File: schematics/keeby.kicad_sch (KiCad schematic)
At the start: 58 parts, among them SW1 SW_Push, SW10 SW_Push, SW11 SW_Push, SW12 SW_Push, SW13 SW_Push, SW14 SW_Push, SW15 SW_Push, SW16 SW_Push, SW17 SW_Push, SW18 SW_Push, SW19 SW_Push, SW2 SW_Push, SW20 SW_Push, SW21 SW_Push, SW22 SW_Push, SW23 SW_Push, SW24 SW_Push, SW25 SW_Push, SW26 SW_Push, SW27 SW_Push, SW28 SW_Push, SW3 SW_Push, SW4 SW_Push, SW5 SW_Push, SW6 SW_Push, SW7 SW_Push, SW8 SW_Push, SW9 SW_Push

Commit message: journaling + more schematic
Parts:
- added D29, D30, D31, D32, D33, D34, D35, D36, D37, D38, D39, D40, D41, D42, D43, D44, D45, D46, D47, D48, D49, D50, D51, D52, D53, D54, D55, D56, D57, D58, D59, D61, D63, D65, D67, D68, D69, D70, D71: 1N4148, Diode_THT:D_DO-35_SOD27_P7.62mm_Horizontal, symbol Diode:1N4148
- added H1, H2, H3, H4: MountingHole, symbol Mechanical:MountingHole
- added S2, S3, S4: MX_stab, PCM_marbastlib-mx:STAB_MX_P_6.25u, symbol PCM_marbastlib-mx:MX_stab
- added SW29, SW30, SW31, SW32, SW33, SW34, SW35, SW36, SW37, SW38, SW39, SW40, SW41, SW42, SW43, SW44, SW45, SW46, SW47, SW48, SW49, SW50, SW51, SW52, SW53, SW54, SW55, SW56, SW57, SW58, SW59, SW61, SW63, SW65, SW67, SW68, SW69, SW70, SW71: SW_Push, symbol Switch:SW_Push
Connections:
- net COL0: now reaches SW1.1
- net COL0: now also A1.7 (GPIO5), SW15.1, SW29.1, SW43.1, SW57.1
- net ROW0: now reaches A1.1 (GPIO0)
- net ROW1: now reaches A1.2 (GPIO1)
- net ROW3: now reaches A1.4 (GPIO2)
- net ROW4: now reaches A1.5 (GPIO3)
- net ROW5: now reaches A1.6 (GPIO4)
- new net: D30.2 (A), SW30.2
- new net: D43.2 (A), SW43.2
- new net: D52.2 (A), SW52.2
- new net: D35.2 (A), SW35.2
- new net: D51.2 (A), SW51.2
- new net: D36.2 (A), SW36.2
- new net: D71.2 (A), SW71.2
- new net: D48.2 (A), SW48.2
- new net: D46.2 (A), SW46.2
- new net: D67.2 (A), SW67.2
- new net: D47.2 (A), SW47.2
- new net: D34.2 (A), SW34.2
- new net: D57.2 (A), SW57.2
- new net: D45.2 (A), SW45.2
- new net: D38.2 (A), SW38.2
- new net: D44.2 (A), SW44.2
- new net: D55.2 (A), SW55.2
- new net: D49.2 (A), SW49.2
- new net: D42.2 (A), SW42.2
- new net: D32.2 (A), SW32.2
- new net: D40.2 (A), SW40.2
- new net: D61.2 (A), SW61.2
- new net: D56.2 (A), SW56.2
- new net: D65.2 (A), SW65.2
- new net: D37.2 (A), SW37.2
- new net: D68.2 (A), SW68.2
- new net: D63.2 (A), SW63.2
- new net: D39.2 (A), SW39.2
- new net: D41.2 (A), SW41.2
- new net: D53.2 (A), SW53.2
- new net: D54.2 (A), SW54.2
- new net: D50.2 (A), SW50.2
- new net: D70.2 (A), SW70.2
- new net: D31.2 (A), SW31.2
- new net: D33.2 (A), SW33.2
- new net: D59.2 (A), SW59.2
- new net: D29.2 (A), SW29.2
- new net: D69.2 (A), SW69.2
- new net: D58.2 (A), SW58.2
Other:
- moved on the sheet: A1, D1, D10, D11, D12, D13, D14, D15, D16, D17, D18, D19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

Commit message: hjalp vro
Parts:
- A1: footprint Module:RaspberryPi_Pico_Common_Unspecified -> Module:RaspberryPi_Pico_Common_THT
- S1, S2, S3, S4: footprint PCM_marbastlib-mx:STAB_MX_P_6.25u -> PCM_marbastlib-mx:STAB_MX_2.25u
- SW1, SW10, SW11, SW12, SW13, SW14, SW15, SW16, SW17, SW18, SW19, SW2, SW20, SW21, SW22, SW23, SW24, SW25, SW26, SW27, SW28, SW29, SW3, SW30, SW31, SW32, SW33, SW34, SW35, SW36, SW37, SW38, SW39, SW4, SW40, SW41, SW42, SW43, SW44, SW45, SW46, SW47, SW48, SW49, SW5, SW50, SW51, SW52, SW53, SW54, SW55, SW56, SW57, SW58, SW59, SW6, SW61, SW63, SW65, SW67, SW68, SW69, SW7, SW70, SW71, SW8, SW9: footprint (none) -> PCM_marbastlib-mx:SW_MX_1u
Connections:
- net ROW0: now also D1.1 (K), D10.1 (K), D11.1 (K), D12.1 (K), D13.1 (K), D14.1 (K), D2.1 (K), D3.1 (K), D4.1 (K), D5.1 (K), D6.1 (K), D7.1 (K), D8.1 (K), D9.1 (K)
- net ROW1: now also D15.1 (K), D16.1 (K), D17.1 (K), D18.1 (K), D19.1 (K), D20.1 (K), D21.1 (K), D22.1 (K), D23.1 (K), D24.1 (K), D25.1 (K), D26.1 (K), D27.1 (K), D28.1 (K)
- net ROW3: now also D29.1 (K), D30.1 (K), D31.1 (K), D32.1 (K), D33.1 (K), D34.1 (K), D35.1 (K), D36.1 (K), D37.1 (K), D38.1 (K), D39.1 (K), D40.1 (K), D41.1 (K), D42.1 (K)
- net ROW4: now also D43.1 (K), D44.1 (K), D45.1 (K), D46.1 (K), D47.1 (K), D48.1 (K), D49.1 (K), D50.1 (K), D51.1 (K), D52.1 (K), D53.1 (K), D54.1 (K), D55.1 (K), D56.1 (K)
- net ROW5: now also D57.1 (K), D58.1 (K), D59.1 (K), D61.1 (K), D63.1 (K), D65.1 (K), D67.1 (K), D68.1 (K), D69.1 (K), D70.1 (K), D71.1 (K)
- net COL1: now reaches SW30.1
- net COL1: now also A1.9 (GPIO6), SW16.1, SW2.1, SW44.1, SW58.1
- net COL2: now reaches SW45.1
- net COL2: now also A1.10 (GPIO7), SW17.1, SW3.1, SW31.1, SW59.1
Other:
- moved on the sheet: A1

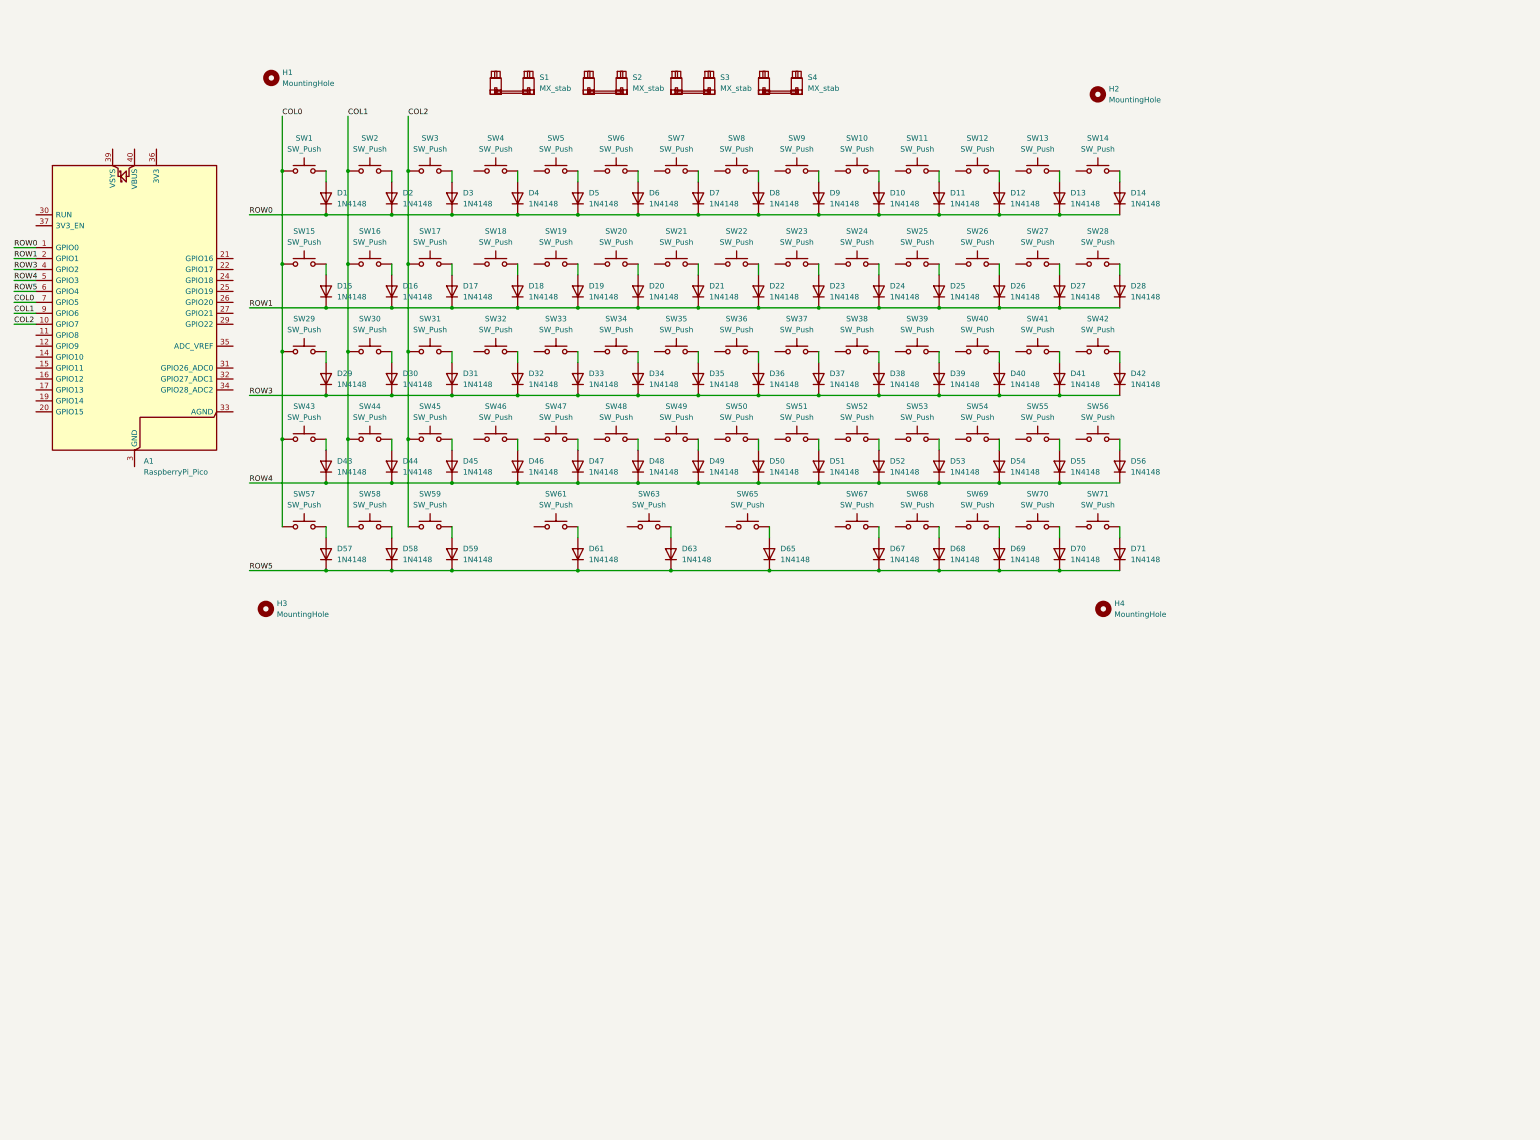
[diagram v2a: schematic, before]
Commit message: 15 columns and 5 rows
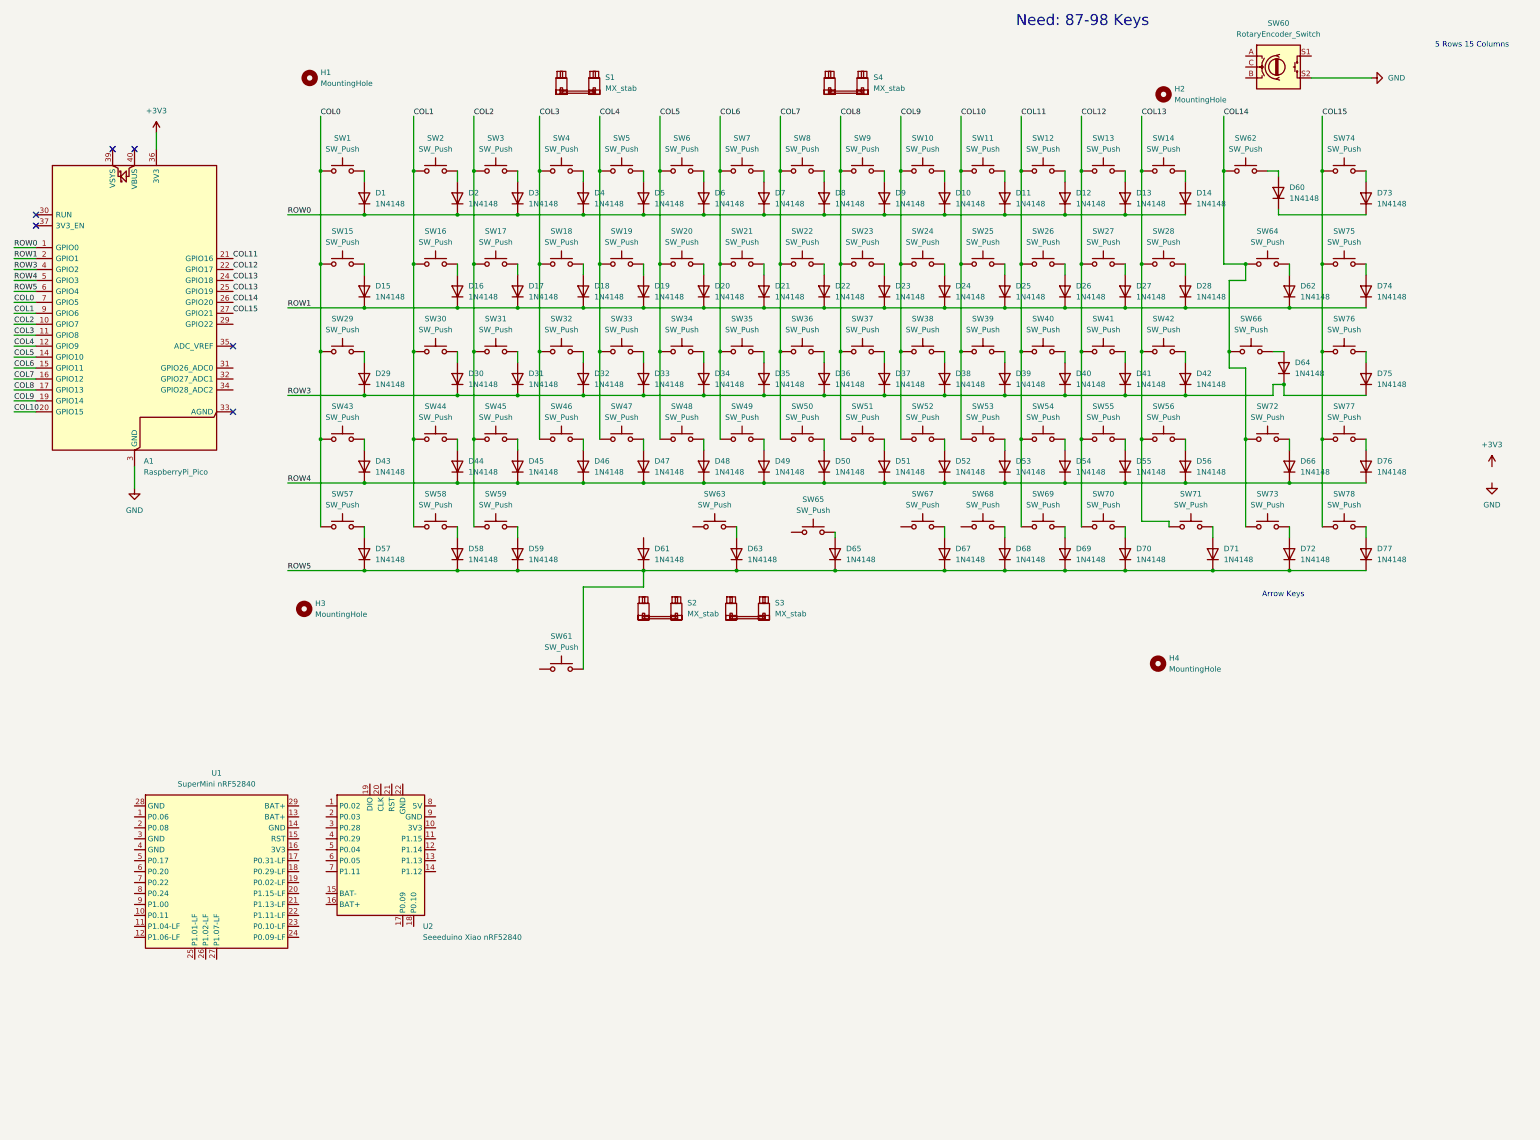
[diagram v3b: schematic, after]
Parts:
- added D60, D62, D64, D66, D72, D73, D74, D75, D76, D77: 1N4148, Diode_THT:D_DO-35_SOD27_P7.62mm_Horizontal, symbol Diode:1N4148
- added SW60: RotaryEncoder_Switch, symbol Device:RotaryEncoder_Switch
- added SW62, SW64, SW66, SW72, SW73, SW74, SW75, SW76, SW77, SW78: SW_Push, PCM_marbastlib-mx:SW_MX_1u, symbol Switch:SW_Push
- added U1: SuperMini nRF52840, PCM_marbastlib-xp-promicroish:SuperMini_nRF52840_AH_USBup, symbol PCM_marbastlib-promicroish:SuperMini_nRF52840
- added U2: Seeeduino Xiao nRF52840, PCM_marbastlib-xp-promicroish:Xiao_nRF52840_ACH, symbol PCM_marbastlib-promicroish:Seeeduino_Xiao_nRF52840
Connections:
- net ROW1: now also D62.1 (K), D74.1 (K)
- net ROW3: now also D64.1 (K), D75.1 (K)
- net ROW4: now also D66.1 (K), D76.1 (K)
- net ROW5: now also SW61.2, D72.1 (K), D77.1 (K)
- net COL9: now reaches SW52.1
- net COL9: now also A1.19 (GPIO14), SW10.1, SW24.1, SW38.1
- net COL3: now reaches SW18.1
- net COL3: now also A1.11 (GPIO8), SW32.1, SW4.1, SW46.1
- net COL8: now reaches SW51.1
- net COL8: now also A1.17 (GPIO13), SW23.1, SW37.1, SW9.1
- net COL7: now reaches SW36.1
- net COL7: now also A1.16 (GPIO12), SW22.1, SW50.1, SW8.1
- net COL4: now reaches SW47.1
- net COL4: now also A1.12 (GPIO9), SW19.1, SW33.1, SW5.1
- net COL6: now reaches SW7.1
- net COL6: now also A1.15 (GPIO11), SW21.1, SW35.1, SW49.1
- net COL12: now reaches SW13.1
- net COL12: now also A1.22 (GPIO17), SW27.1, SW41.1, SW55.1, SW70.1
- net COL11: now reaches SW12.1
- net COL11: now also A1.21 (GPIO16), SW26.1, SW40.1, SW54.1, SW69.1
- net COL13: now reaches SW42.1
- net COL13: now also A1.24 (GPIO18), A1.25 (GPIO19), SW14.1, SW28.1, SW56.1, SW71.1
- net at D61.2 (A): no longer SW61.2
- net COL10: now reaches SW39.1
- net COL10: now also A1.20 (GPIO15), SW11.1, SW25.1, SW53.1
- net COL5: now reaches SW48.1
- net COL5: now also A1.14 (GPIO10), SW20.1, SW34.1, SW6.1
- net GND: now reaches A1.13 (GND), A1.18 (GND), A1.23 (GND), A1.28 (GND), A1.3 (GND), A1.38 (GND), A1.8 (GND)
- net GND: now also SW60.S2
- net COL14: now reaches A1.26 (GPIO20)
- net COL14: now also SW62.1, SW64.1, SW66.1, SW72.1, SW73.1
- net COL15: now reaches A1.27 (GPIO21)
- net COL15: now also SW74.1, SW75.1, SW76.1, SW77.1, SW78.1
- net +3V3: now reaches A1.36 (3V3)
- new net: D62.2 (A), SW64.2
- new net: D72.2 (A), SW73.2
- new net: D64.2 (A), SW66.2
- new net: D66.2 (A), SW72.2
- new net: D60.2 (A), SW62.2
- new net: D75.2 (A), SW76.2
- new net: D74.2 (A), SW75.2
- new net: D60.1 (K), D73.1 (K)
- new net: D73.2 (A), SW74.2
- new net: D77.2 (A), SW78.2
- new net: D76.2 (A), SW77.2
- no-connect marks 0 -> 6
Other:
- note added: "5 Rows 15 Columns"
- note added: "Arrow Keys"
- note added: "Need: 87-98 Keys"
- moved on the sheet: D1, D10, D11, D12, D13, D14, D15, D16, D17, D18, D19, D2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

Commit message: laid out this ratnest is hurting my brain
installed kbplacer to do ts
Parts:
- removed D61, D65: 1N4148, Diode_THT:D_DO-35_SOD27_P7.62mm_Horizontal, symbol Diode:1N4148
- removed SW61, SW65: SW_Push, PCM_marbastlib-mx:SW_MX_1u, symbol Switch:SW_Push
- removed U2: Seeeduino Xiao nRF52840, PCM_marbastlib-xp-promicroish:Xiao_nRF52840_ACH, symbol PCM_marbastlib-promicroish:Seeeduino_Xiao_nRF52840
- added D76, D77: SK6812MINI-E, LED_SMD:LED_SK6812MINI-E_3.2x2.8mm_P1.5mm_ReverseMount, symbol LED:SK6812MINI-E
- added D78: SK6812MINI-E, SK6812MINI-E - 3.2x2.8x1.78mm, symbol SK6812MINI-E:SK6812MINI-E
- added LED1: SK6812MINI-E, PCM_marbastlib-various:LED_6028R, symbol PCM_marbastlib-various:SK6812MINI-E
- S3: footprint PCM_marbastlib-mx:STAB_MX_2.25u -> PCM_marbastlib-mx:STAB_MX_6.25u
- SW76: renamed from SW60; footprint (none) -> PCM_marbastlib-various:ROT_Alps_EC11E-Switch
- renumbered D60 to D1, D9 to D10, D10 to D11, D11 to D12, D12 to D13, D13 to D14, D14 to D15, D73 to D16, D15 to D17, D16 to D18, D17 to D19, D1 to D2, D18 to D20, D19 to D21, D20 to D22, D21 to D23, D22 to D24, D23 to D25, D24 to D26, D25 to D27, D26 to D28, D27 to D29, D2 to D3, D28 to D30, D62 to D31, D74 to D32, D64 to D33, D29 to D34, D30 to D35, D31 to D36, D32 to D37, D33 to D38, D34 to D39, D3 to D4, D35 to D40, D36 to D41, D37 to D42, D38 to D43, D39 to D44, D40 to D45, D41 to D46, D42 to D47, D75 to D48, D43 to D49, D4 to D5, D44 to D50, D45 to D51, D46 to D52, D47 to D53, D48 to D54, D49 to D55, D50 to D56, D51 to D57, D52 to D58, D53 to D59, D5 to D6, D54 to D60, D55 to D61, D56 to D62, D66 to D63, D76 to D64, D57 to D65, D58 to D66, D59 to D67, D63 to D68, D67 to D69, D6 to D7, D68 to D70, D69 to D71, D70 to D72, D71 to D73, D72 to D74, D77 to D75, D7 to D8, D8 to D9, S4 to S2, S2 to S4, SW62 to SW15, SW74 to SW16, SW15 to SW17, SW16 to SW18, SW17 to SW19, SW18 to SW20, SW19 to SW21, SW20 to SW22, SW21 to SW23, SW22 to SW24, SW23 to SW25, SW24 to SW26, SW25 to SW27, SW26 to SW28, SW27 to SW29, SW28 to SW30, SW64 to SW31, SW75 to SW32, SW29 to SW33, SW30 to SW34, SW31 to SW35, SW32 to SW36, SW33 to SW37, SW34 to SW38, SW35 to SW39, SW36 to SW40, SW37 to SW41, SW38 to SW42, SW39 to SW43, SW40 to SW44, SW41 to SW45, SW42 to SW46, SW66 to SW47, SW76 to SW48, SW43 to SW49, SW44 to SW50, SW45 to SW51, SW46 to SW52, SW47 to SW53, SW48 to SW54, SW49 to SW55, SW50 to SW56, SW51 to SW57, SW52 to SW58, SW53 to SW59, SW54 to SW60, SW55 to SW61, SW56 to SW62, SW72 to SW63, SW77 to SW64, SW57 to SW65, SW58 to SW66, SW59 to SW67, SW63 to SW68, SW67 to SW69, SW68 to SW70, SW69 to SW71, SW70 to SW72, SW71 to SW73, SW73 to SW74, SW78 to SW75
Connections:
- net +3V3: now also D76.3 (VDD), D77.3 (VDD)
- net COL10: now also SW70.1
- net COL4: now also SW68.1
- net COL9: now also SW69.1
- net GND: now also SW76.C, SW76.S1, D76.1 (VSS), D77.1 (VSS); no longer SW76.S2
- new net: D76.4 (DOUT), D77.2 (DIN)
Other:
- company: (none) -> Me
- title: (none) -> Kai-Keeby
- moved on the sheet: A1, D1, D10, D11, D12, D13, D14, D15, D16, D17, D18, D19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

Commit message: I have narrowed down the headache of all the keys. I can route peacefully now.
+maybe some uncommitted changes from a few days ago as well...
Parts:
- removed D16, D32, D48, D64, D75: 1N4148, Diode_THT:D_DO-35_SOD27_P7.62mm_Horizontal, symbol Diode:1N4148
- removed SW16, SW32, SW48, SW64, SW75: SW_Push, PCM_marbastlib-mx:SW_MX_1u, symbol Switch:SW_Push
- renumbered D17 to D16, D18 to D17, D19 to D18, D20 to D19, D21 to D20, D22 to D21, D23 to D22, D24 to D23, D25 to D24, D26 to D25, D27 to D26, D28 to D27, D29 to D28, D30 to D29, D31 to D30, D33 to D31, D34 to D32, D35 to D33, D36 to D34, D37 to D35, D38 to D36, D39 to D37, D40 to D38, D41 to D39, D42 to D40, D43 to D41, D44 to D42, D45 to D43, D47 to D44, D56 to D45, D58 to D46, D49 to D47, D50 to D48, D51 to D49, D52 to D50, D53 to D51, D54 to D52, D55 to D53, D57 to D54, D59 to D55, D61 to D56, D62 to D57, D63 to D58, D65 to D59, D66 to D60, D67 to D61, D68 to D62, D69 to D63, D70 to D64, D71 to D65, D72 to D66, D73 to D67, D74 to D68, D60 to D69, D46 to D70, D78 to D71, D76 to LED1, D77 to LED2, LED1 to LED3, S3 to S2, S2 to S3, SW17 to SW16, SW18 to SW17, SW19 to SW18, SW20 to SW19, SW21 to SW20, SW22 to SW21, SW23 to SW22, SW24 to SW23, SW25 to SW24, SW26 to SW25, SW27 to SW26, SW28 to SW27, SW29 to SW28, SW30 to SW29, SW31 to SW30, SW33 to SW31, SW34 to SW32, SW35 to SW33, SW36 to SW34, SW37 to SW35, SW38 to SW36, SW39 to SW37, SW40 to SW38, SW41 to SW39, SW42 to SW40, SW43 to SW41, SW44 to SW42, SW46 to SW43, SW47 to SW44, SW49 to SW45, SW50 to SW46, SW51 to SW47, SW52 to SW48, SW53 to SW49, SW54 to SW50, SW55 to SW51, SW56 to SW52, SW57 to SW53, SW58 to SW54, SW59 to SW55, SW61 to SW56, SW62 to SW57, SW63 to SW58, SW65 to SW59, SW66 to SW60, SW67 to SW61, SW69 to SW62, SW70 to SW63, SW71 to SW64, SW68 to SW65, SW72 to SW66, SW73 to SW67, SW74 to SW68, SW76 to SW69, SW60 to SW70, SW45 to SW71
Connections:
- net COL10: now also SW64.1; no longer SW63.1
- net COL11: no longer SW64.1, SW70.1
- net COL12: no longer SW71.1
- net COL4: no longer SW65.1
- net COL5: now also SW65.1
- net COL8: now also SW62.1
- net COL9: now also SW63.1; no longer SW62.1
- net ROW0: now also D1.1 (K)
- net ROW3: no longer D70.1 (K)
- net ROW4: no longer D69.1 (K)
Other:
- moved on the sheet: D1, D10, D11, D12, D13, D14, D15, D16, D17, D18, D19, D2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

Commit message: more hours of work
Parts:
- removed D69, D70: 1N4148, Diode_THT:D_DO-35_SOD27_P7.62mm_Horizontal, symbol Diode:1N4148
- removed SW70, SW71: SW_Push, PCM_marbastlib-mx:SW_MX_1u, symbol Switch:SW_Push
- added JS1: joystick_analog, PCM_marbastlib-various:joystick_psp1000, symbol PCM_marbastlib-various:joystick_analog
- S2: renamed from S1; footprint PCM_marbastlib-mx:STAB_MX_2.25u -> PCM_marbastlib-mx:STAB_MX_2u
- renumbered D71 to D69, SW69 to EC1, S4 to S1, S2 to S4
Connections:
- net COL10: now also SW65.1; no longer SW64.1
- net COL13: no longer A1.25 (GPIO19)
- net COL14: now also A1.25 (GPIO19); no longer A1.26 (GPIO20)
- net COL15: no longer A1.27 (GPIO21)
- net COL5: now also SW62.1; no longer SW65.1
- net COL8: now also SW63.1; no longer SW62.1
- net COL9: now also SW64.1; no longer SW63.1
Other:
- moved on the sheet: D62, D63, D64, D65, SW62, SW63, SW64, SW65

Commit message: checkpointer. readme stuff. more journal. fix switch order
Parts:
- removed D69: SK6812MINI-E, SK6812MINI-E - 3.2x2.8x1.78mm, symbol SK6812MINI-E:SK6812MINI-E
- removed LED3: SK6812MINI-E, PCM_marbastlib-various:LED_6028R, symbol PCM_marbastlib-various:SK6812MINI-E
- JS1: footprint PCM_marbastlib-various:joystick_psp1000 -> PCM_marbastlib-xp-various:PNT_psp1000
- renumbered D2 to D1, D11 to D10, D12 to D11, D13 to D12, D14 to D13, D15 to D14, D1 to D15, D3 to D2, D4 to D3, D32 to D31, D33 to D32, D34 to D33, D35 to D34, D36 to D35, D37 to D36, D38 to D37, D39 to D38, D40 to D39, D5 to D4, D41 to D40, D42 to D41, D43 to D42, D44 to D43, D31 to D44, D6 to D5, D7 to D6, D63 to D62, D64 to D63, D65 to D64, D62 to D65, D8 to D7, D9 to D8, D10 to D9
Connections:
- net +3V3: now also JS1.4 (VCC)
- net GND: now also JS1.2 (GND)
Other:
- moved on the sheet: A1, D15, D44, JS1, LED1, LED2, U1

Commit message: connected the nrf to the column/rows.
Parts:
- added U2: MCP23017x-x-SP, Package_DIP:DIP-28_W7.62mm, symbol Interface_Expansion:MCP23017x-x-SP
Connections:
- net +3V3: now also U1.15 (RST); no longer A1.36 (3V3)
- net COL0: now also U1.8 (P0.24); no longer A1.7 (GPIO5)
- net COL1: now also U1.9 (P1.00); no longer A1.9 (GPIO6)
- net COL10: now also U1.22 (P1.11-LF); no longer A1.20 (GPIO15)
- net COL11: now also U1.23 (P0.10-LF); no longer A1.21 (GPIO16)
- net COL12: now also U1.24 (P0.09-LF); no longer A1.22 (GPIO17)
- net COL13: now also U1.27 (P1.07-LF); no longer A1.24 (GPIO18)
- net COL14: now also U1.26 (P1.02-LF); no longer A1.25 (GPIO19)
- net COL2: now also U1.10 (P0.11); no longer A1.10 (GPIO7)
- net COL3: now also U1.11 (P1.04-LF); no longer A1.11 (GPIO8)
- net COL4: now also U1.12 (P1.06-LF); no longer A1.12 (GPIO9)
- net COL5: now also U1.17 (P0.31-LF); no longer A1.14 (GPIO10)
- net COL6: now also U1.18 (P0.29-LF); no longer A1.15 (GPIO11)
- net COL7: now also U1.19 (P0.02-LF); no longer A1.16 (GPIO12)
- net COL8: now also U1.20 (P1.15-LF); no longer A1.17 (GPIO13)
- net COL9: now also U1.21 (P1.13-LF); no longer A1.19 (GPIO14)
- net GND: now also U1.14 (GND), U1.28 (GND), U1.3 (GND), U1.4 (GND); no longer A1.13 (GND), A1.18 (GND), A1.23 (GND), A1.28 (GND), A1.3 (GND), A1.38 (GND), A1.8 (GND)
- net ROW0: now also U1.1 (P0.06); no longer A1.1 (GPIO0)
- net ROW1: now also U1.2 (P0.08); no longer A1.2 (GPIO1)
- net ROW3: now also U1.5 (P0.17); no longer A1.4 (GPIO2)
- net ROW4: now also U1.6 (P0.20); no longer A1.5 (GPIO3)
- net ROW5: now also U1.7 (P0.22); no longer A1.6 (GPIO4)
- new net: A1.13 (GND), A1.18 (GND), A1.23 (GND), A1.28 (GND), A1.3 (GND), A1.38 (GND), A1.8 (GND)
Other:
- note added: "Joystick"
- moved on the sheet: A1, EC1, JS1, LED1, LED2, S1, S3, U1
